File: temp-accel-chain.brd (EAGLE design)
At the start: 29.8 x 10.5 mm, 9 parts, among them U1 ADT7420UCPZ-R2

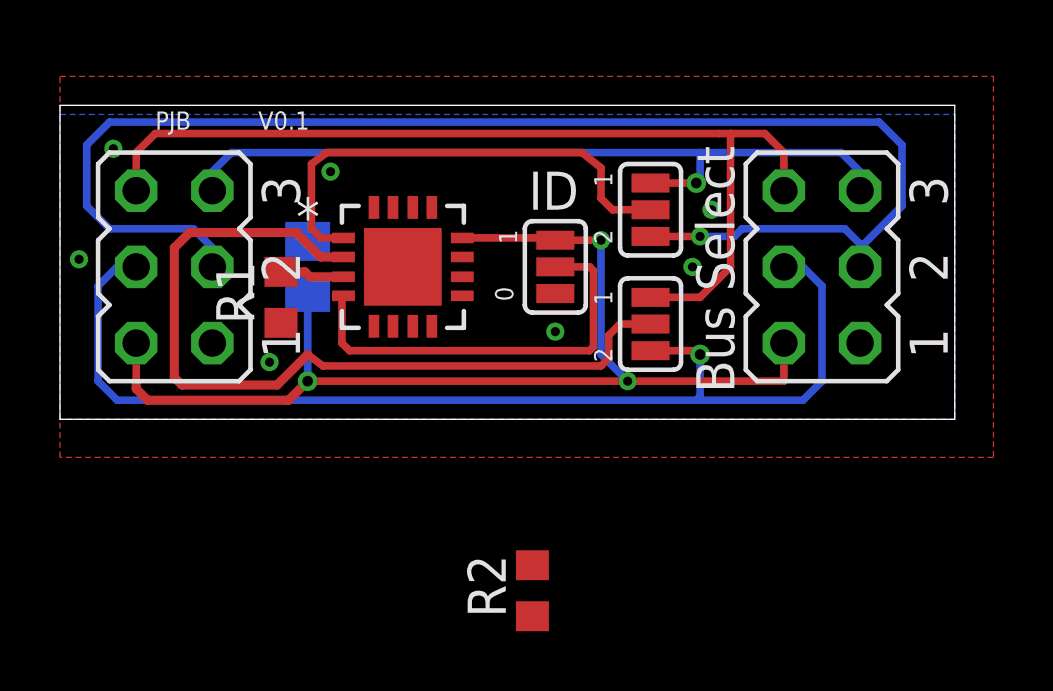
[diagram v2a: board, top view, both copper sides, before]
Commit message: temp i2c address either 00 or 11 thus saving a resistor
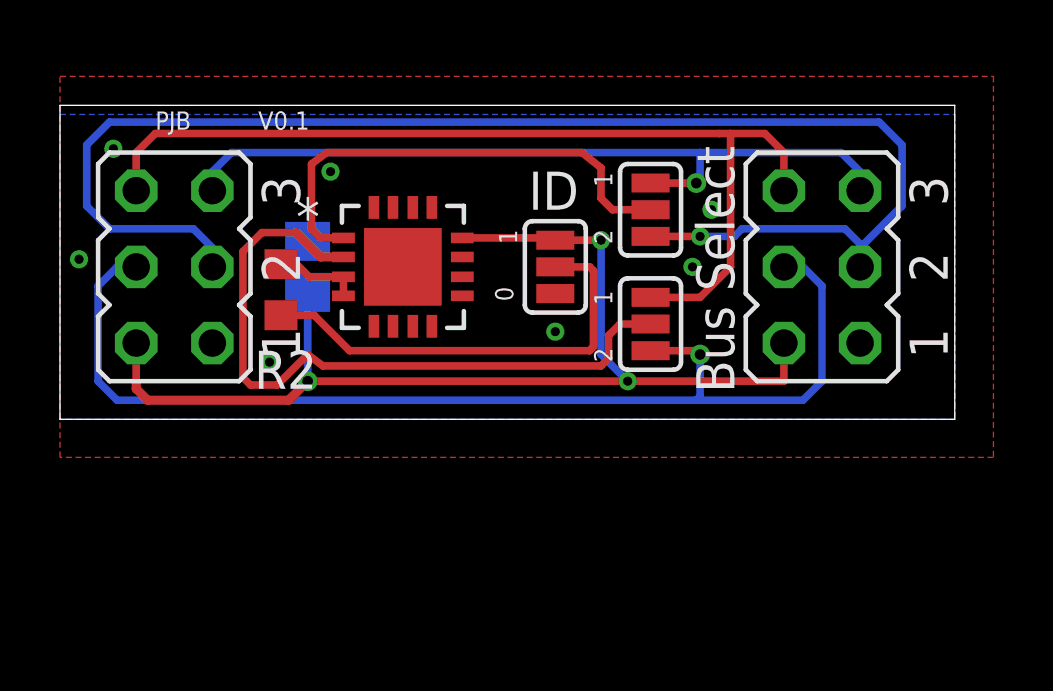
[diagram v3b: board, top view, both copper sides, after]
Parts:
- removed R1: 10K, resistor:R0603
- moved R2 13.1 mm to (8.64, 4.32)
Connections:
- removed net N$1: R1.2, U1.3
- removed net N$3: R2.2, U1.4
- new net ADD_SEL: JP5.2, R2.1
- net ADD: now also R2.2, U1.3, U1.4; no longer JP5.2, R2.1
- net VCC: no longer R1.1
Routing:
- net ADD_SEL: track 0.00 -> 14.8 mm
- net ADD: track 13.9 -> 2.89 mm
- net SDA: track 28.1 -> 23.4 mm
- net N$1: track 2.15 -> 0.00 mm
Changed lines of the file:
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@@
 <attribute name="VALUE" x="17.78" y="4.9799" size="0.02" layer="27" rot="R90"/>
 </element>
-<element name="R1" library="resistor" package="R0603" value="10K" x="8.636" y="4.064" smashed="yes" rot="R90">
-<attribute name="NAME" x="7.747" y="3.175" size="1.27" layer="25" rot="R90"/>
+<element name="R2" library="resistor" package="R0603" value="10K" x="8.636" y="4.318" smashed="yes" rot="R90">
+<attribute name="NAME" x="7.747" y="1.016" size="1.27" layer="25"/>
 </element>
-<element name="R2" library="resistor" package="R0603" value="10K" x="17.018" y="-5.715" rot="R90"/>
 </elements>
 <signals>
@@
 <via x="20.193" y="1.27" extent="1-16" drill="0.3048" diameter="0.508"/>
 <wire x1="20.193" y1="1.27" x2="25.4" y2="1.27" width="0.254" layer="1"/>
-<contactref element="R1" pad="1"/>
 <wire x1="9.525" y1="1.27" x2="8.89" y2="0.635" width="0.3048" layer="1"/>
 <wire x1="8.89" y1="0.635" x2="4.191" y2="0.635" width="0.3048" layer="1"/>
 <wire x1="4.191" y1="0.635" x2="3.81" y2="1.016" width="0.3048" layer="1"/>
 <wire x1="3.81" y1="1.016" x2="3.81" y2="1.27" width="0.3048" layer="1"/>
-<wire x1="9.525" y1="4.23" x2="8.636" y2="3.214" width="0" layer="19" extent="1-16"/>
 </signal>
 <signal name="SCL1">
@@
 <via x="3.048" y="9.017" extent="1-16" drill="0.3048" diameter="0.508"/>
 <via x="22.987" y="6.985" extent="1-16" drill="0.3048" diameter="0.508"/>
-<wire x1="6.35" y1="2.54" x2="1.905" y2="5.334" width="0" layer="19" extent="1-1"/>
 </signal>
 <signal name="SDA">
@@
 <wire x1="19.304" y1="1.778" x2="10.033" y2="1.778" width="0.254" layer="1"/>
 <wire x1="10.033" y1="1.778" x2="9.525" y2="2.159" width="0.254" layer="1"/>
-<wire x1="9.525" y1="2.159" x2="8.509" y2="1.143" width="0.3048" layer="1"/>
-<wire x1="8.509" y1="1.143" x2="5.334" y2="1.143" width="0.3048" layer="1"/>
-<wire x1="5.334" y1="1.143" x2="5.08" y2="1.397" width="0.3048" layer="1"/>
-<wire x1="5.08" y1="1.397" x2="5.08" y2="5.715" width="0.3048" layer="1"/>
-<wire x1="5.08" y1="5.715" x2="5.588" y2="6.223" width="0.3048" layer="1"/>
-<wire x1="5.588" y1="6.223" x2="9.144" y2="6.223" width="0.3048" layer="1"/>
+<wire x1="9.525" y1="2.159" x2="8.509" y2="1.143" width="0.254" layer="1"/>
 <wire x1="10.7188" y1="5.4102" x2="9.9568" y2="5.4102" width="0.3048" layer="1"/>
 <wire x1="9.9568" y1="5.4102" x2="9.144" y2="6.223" width="0.3048" layer="1"/>
+<wire x1="8.509" y1="1.143" x2="7.62" y2="1.143" width="0.254" layer="1"/>
+<wire x1="7.62" y1="1.143" x2="7.366" y2="1.397" width="0.254" layer="1"/>
+<wire x1="7.366" y1="1.397" x2="7.366" y2="5.588" width="0.254" layer="1"/>
+<wire x1="7.366" y1="5.588" x2="8.001" y2="6.223" width="0.254" layer="1"/>
+<wire x1="8.001" y1="6.223" x2="9.144" y2="6.223" width="0.254" layer="1"/>
 </signal>
 <signal name="SCL">
@@
 </signal>
 <signal name="ADD">
+<contactref element="R2" pad="2"/>
+<contactref element="U1" pad="4"/>
+<contactref element="U1" pad="3"/>
+<wire x1="10.7188" y1="4.1148" x2="10.7188" y2="4.7498" width="0.254" layer="1"/>
+<wire x1="8.636" y1="5.168" x2="9.1576" y2="5.168" width="0.254" layer="1"/>
+<wire x1="9.1576" y1="5.168" x2="9.5758" y2="4.7498" width="0.254" layer="1"/>
+<wire x1="9.5758" y1="4.7498" x2="10.7188" y2="4.7498" width="0.254" layer="1"/>
+</signal>
+<signal name="ADD_SEL">
+<contactref element="R2" pad="1"/>
 <contactref element="JP5" pad="2"/>
 <wire x1="17.78" y1="5.08" x2="18.923" y2="5.08" width="0.254" layer="1"/>
-<wire x1="10.922" y1="2.286" x2="10.668" y2="2.54" width="0.254" layer="1"/>
-<wire x1="10.668" y1="2.54" x2="10.668" y2="4.064" width="0.254" layer="1"/>
 <wire x1="10.922" y1="2.286" x2="18.923" y2="2.286" width="0.254" layer="1"/>
 <wire x1="18.923" y1="2.286" x2="19.05" y2="2.413" width="0.254" layer="1"/>
 <wire x1="19.05" y1="2.413" x2="19.05" y2="4.953" width="0.254" layer="1"/>
 <wire x1="19.05" y1="4.953" x2="18.923" y2="5.08" width="0.254" layer="1"/>
-<contactref element="R2" pad="1"/>
-<wire x1="17.018" y1="-6.565" x2="18.923" y2="2.286" width="0" layer="19" extent="1-1"/>
-</signal>
-<signal name="N$1">
-<contactref element="U1" pad="3"/>
-<contactref element="R1" pad="2"/>
-<wire x1="8.636" y1="4.914" x2="9.437" y2="4.914" width="0.3048" layer="1"/>
-<wire x1="9.437" y1="4.914" x2="9.6012" y2="4.7498" width="0.3048" layer="1"/>
-<wire x1="9.6012" y1="4.7498" x2="10.7188" y2="4.7498" width="0.3048" layer="1"/>
-</signal>
-<signal name="N$3">
-<contactref element="R2" pad="2"/>
-<contactref element="U1" pad="4"/>
-<wire x1="10.7188" y1="4.1148" x2="17.018" y2="-4.865" width="0" layer="19" extent="1-1"/>
+<wire x1="8.636" y1="3.468" x2="9.74" y2="3.468" width="0.254" layer="1"/>
+<wire x1="9.74" y1="3.468" x2="10.922" y2="2.286" width="0.254" layer="1"/>
 </signal>
 </signals>
